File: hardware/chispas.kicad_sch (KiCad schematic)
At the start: 25 parts, among them J1 Conn_01x05, J2 Conn_01x04, J3 Conn_01x04, J4 Conn_01x06, J5 Conn_01x02, U1 Heltec_WiFi_LoRa_32_V3, U2 PC817X2CSP9F, U3 PAM8302AASCR

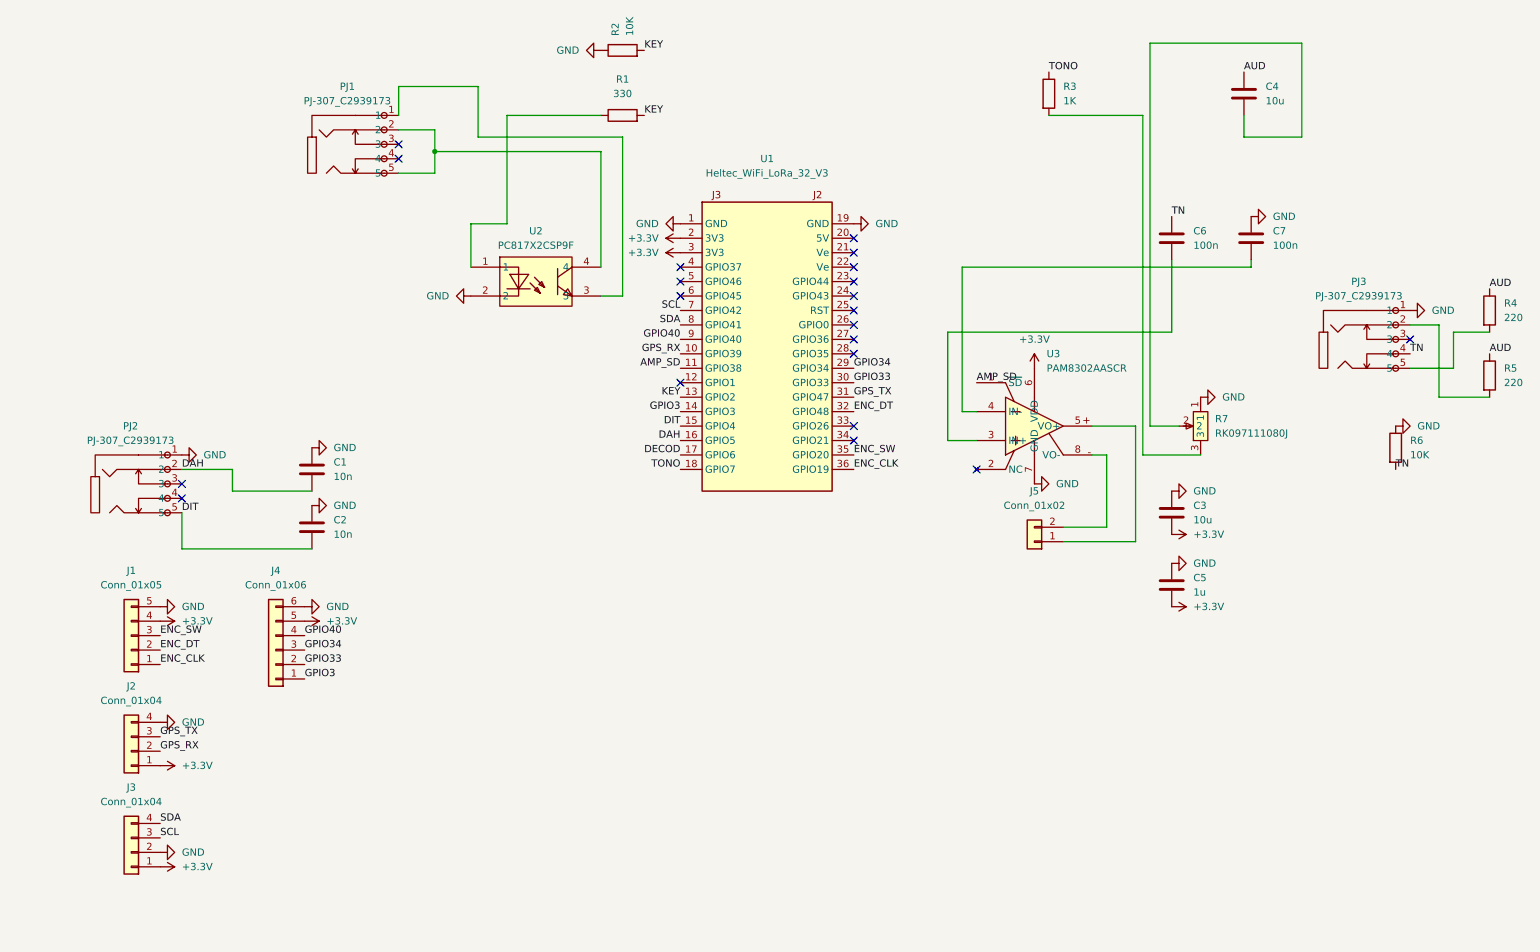
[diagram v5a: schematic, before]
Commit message: PCB: esquema completo (decodificador con puentes para trafo; ERC sin avisos)
Co-Authored-By: Claude Opus 5.5 <noreply@anthropic.com>
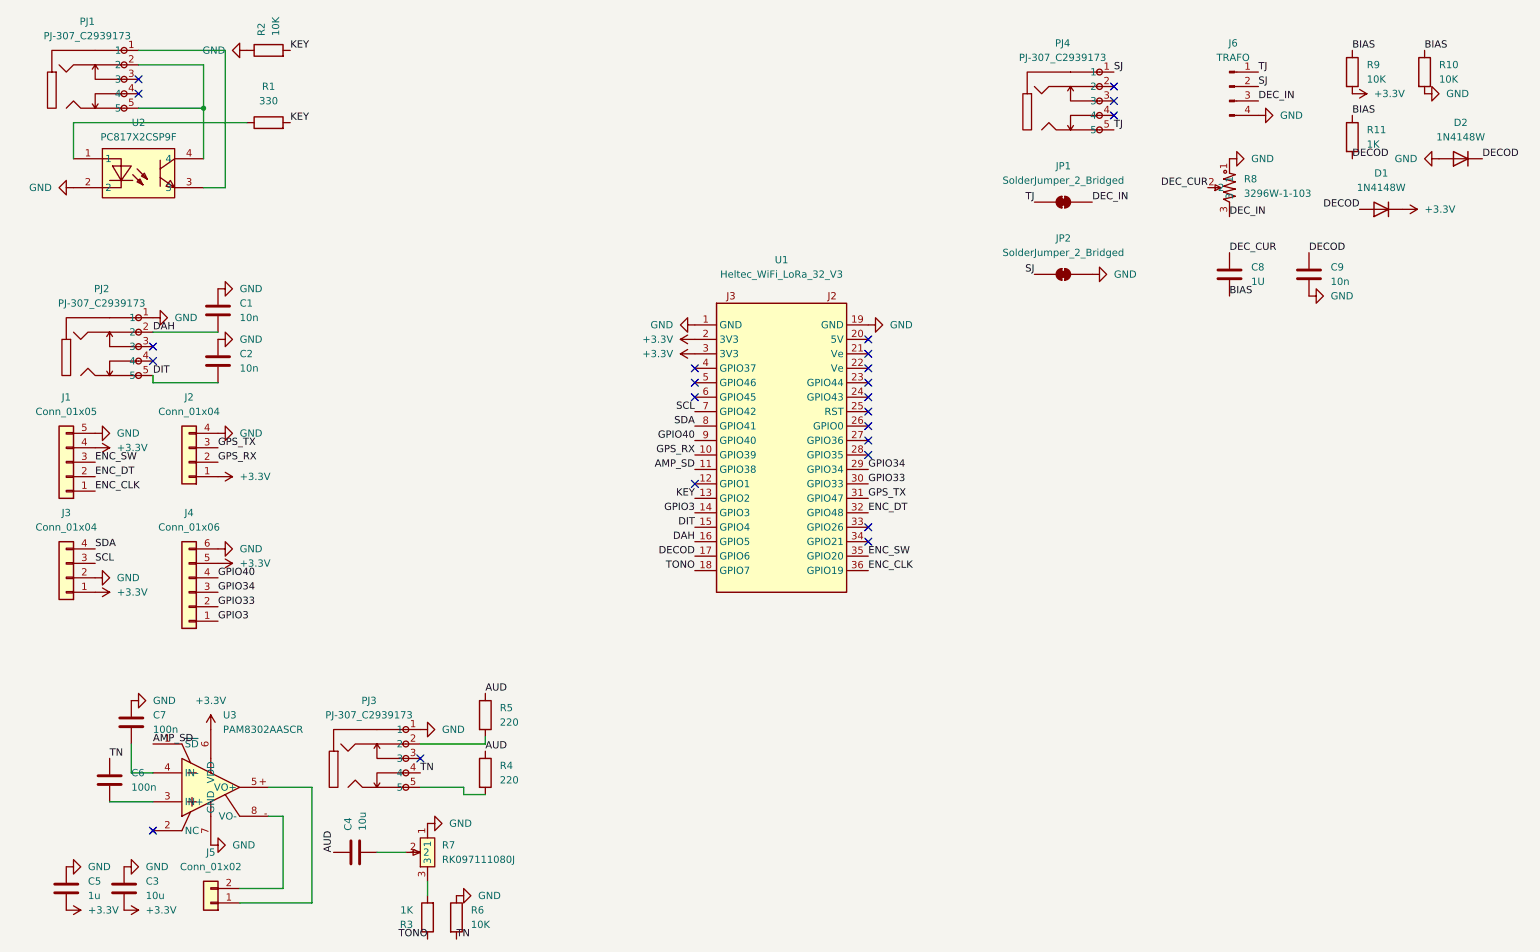
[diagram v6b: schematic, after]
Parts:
- added C8: 1U, Capacitor_SMD:C_0805_2012Metric, symbol Device:C
- added C9: 10n, Capacitor_SMD:C_0805_2012Metric, symbol Device:C
- added D1, D2: 1N4148W, Diode_SMD:D_SOD-123, symbol Device:D
- added J6: TRAFO, Connector_PinHeader_2.54mm:PinHeader_1x04_P2.54mm_Vertical, symbol Connector:Conn_01x04_Pin
- added JP1, JP2: SolderJumper_2_Bridged, Jumper:SolderJumper-2_P1.3mm_Bridged_RoundedPad1.0x1.5mm, symbol Jumper:SolderJumper_2_Bridged
- added PJ4: PJ-307_C2939173, chispas:AUDIO-TH_PJ-307, symbol chispas:PJ-307_C2939173
- added R10, R9: 10K, Resistor_SMD:R_0805_2012Metric, symbol Device:R
- added R11: 1K, Resistor_SMD:R_0805_2012Metric, symbol Device:R
- added R8: 3296W-1-103, chispas:RES-ADJ-TH_3P-L10.0-W10.0-P2.50-L, symbol chispas:3296W-1-103
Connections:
- net +3.3V: now also D1.1 (K), R9.2
- net DECOD: now also C9.1, D1.2 (A), D2.1 (K), R11.2
- net GND: now also C9.2, D2.2 (A), J6.4 (Pin_4), JP2.2 (B), R10.2, R8.1
- new net BIAS: C8.2, R10.1, R11.1, R9.1
- new net DEC_CUR: C8.1, R8.2
- new net DEC_IN: J6.3 (Pin_3), JP1.2 (B), R8.3
- new net SJ: J6.2 (Pin_2), JP2.1 (A), PJ4.1
- new net TJ: J6.1 (Pin_1), JP1.1 (A), PJ4.5
- no-connect marks 21 -> 24
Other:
- moved on the sheet: C1, C2, C3, C4, C5, C6, C7, J1, J2, J3, J4, J5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

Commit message: PCB: placa de 90x60 mm, primera colocacion (colocar.py) y agujeros de los jacks sin metalizar
Co-Authored-By: Claude Opus 5.5 <noreply@anthropic.com>
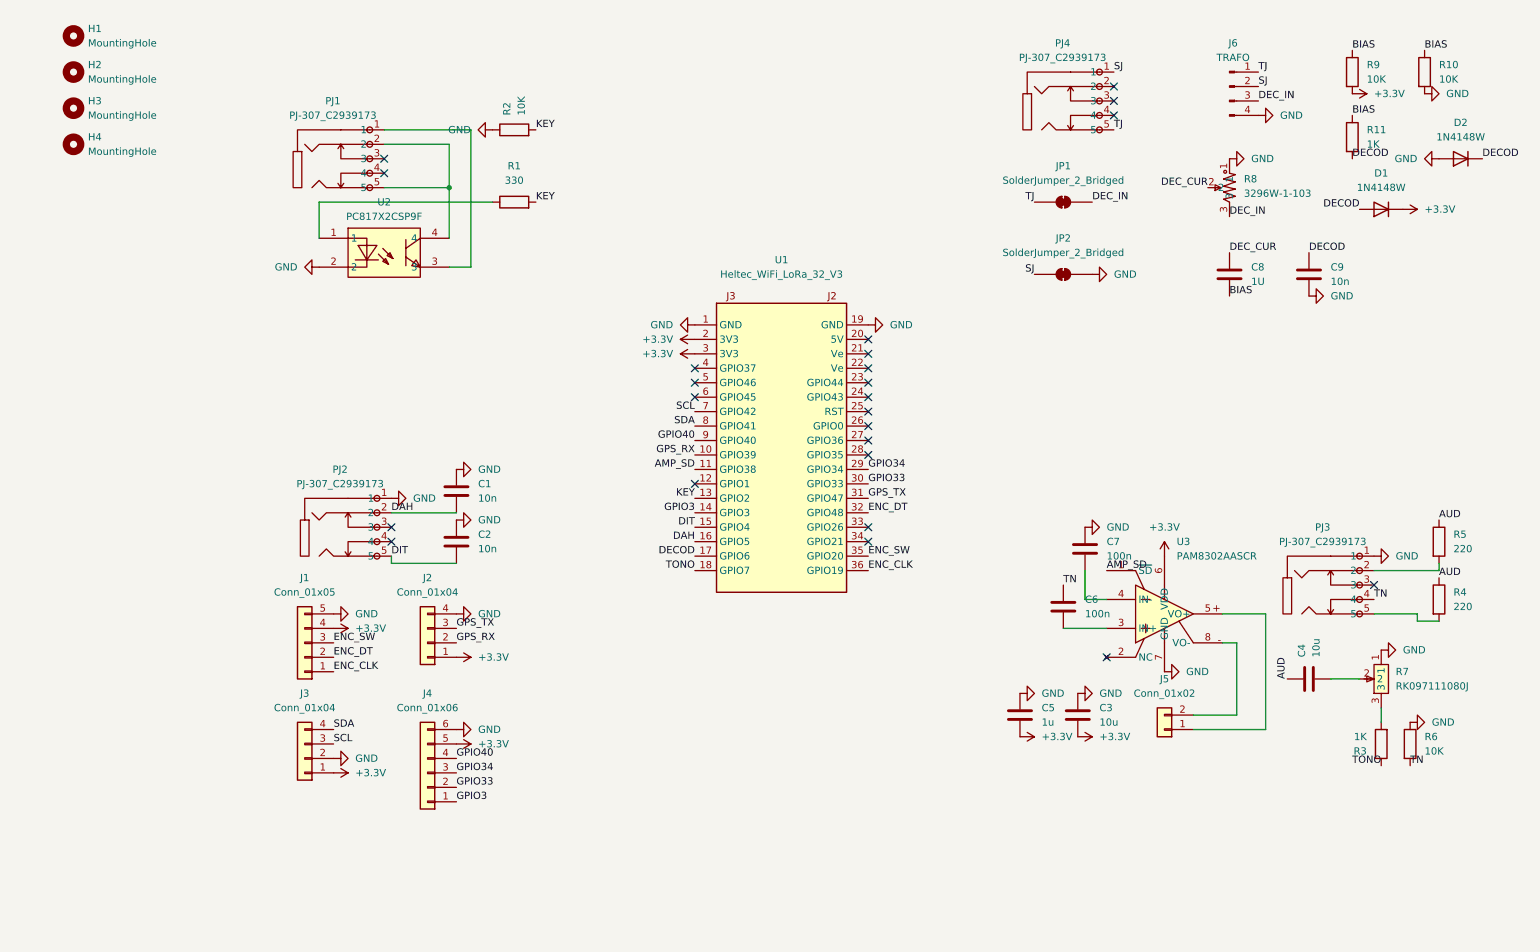
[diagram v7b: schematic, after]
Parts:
- added H1, H2, H3, H4: MountingHole, MountingHole:MountingHole_3.2mm_M3, symbol Mechanical:MountingHole
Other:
- moved on the sheet: C1, C2, C3, C4, C5, C6, C7, J1, J2, J3, J4, J5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

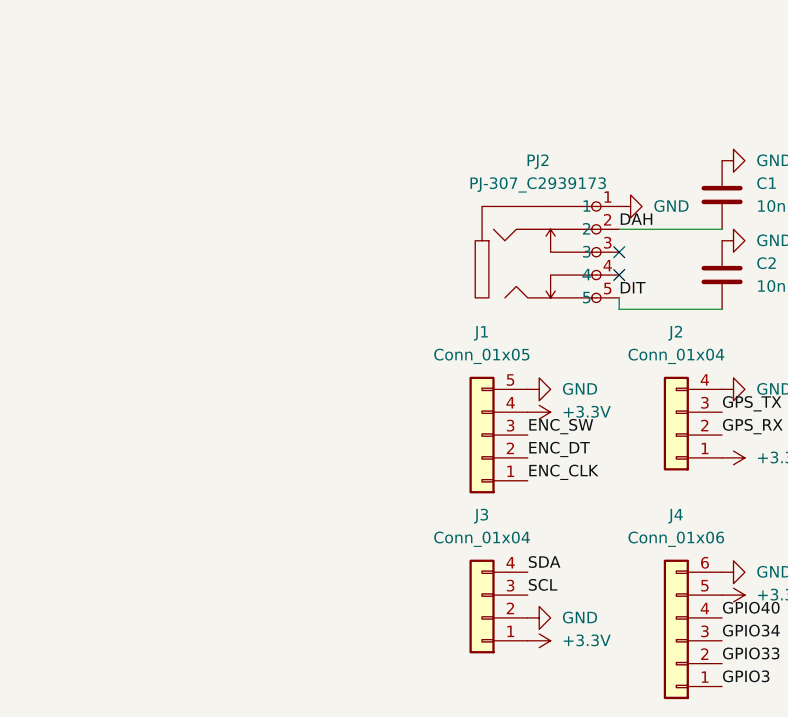
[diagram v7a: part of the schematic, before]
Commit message: PCB: encoder Bourns PEC11R-4230F-S0024 en la placa (24/24, eje 30 mm) con el filtro RC de Bourns; tipos_pines: pasivos por defecto
Co-Authored-By: Claude Opus 5.5 <noreply@anthropic.com>
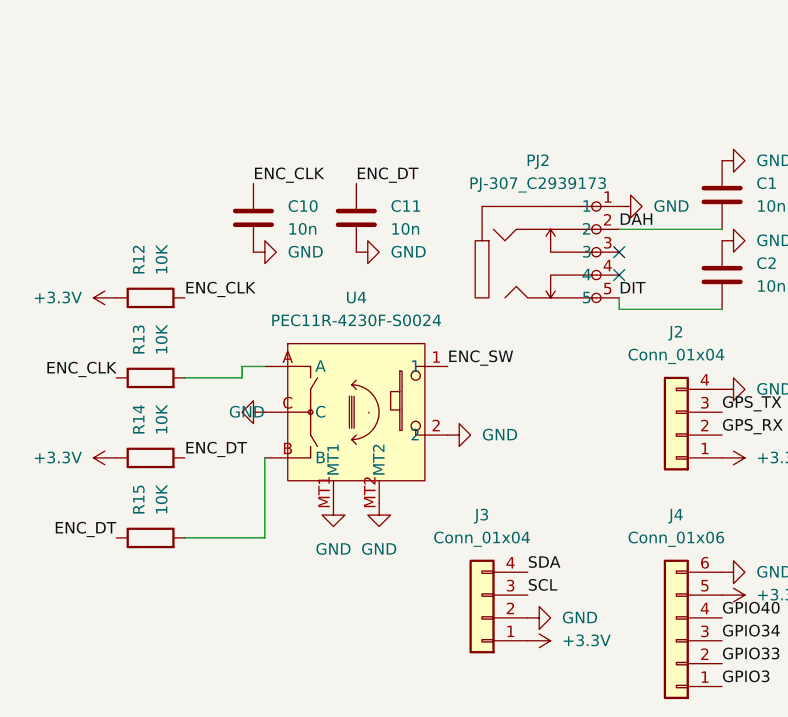
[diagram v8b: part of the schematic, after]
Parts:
- removed J1: Conn_01x05, Connector_JST:JST_XH_B5B-XH-A_1x05_P2.50mm_Vertical, symbol Connector_Generic:Conn_01x05
- added C10, C11: 10n, Capacitor_SMD:C_0805_2012Metric, symbol Device:C
- added R12, R13, R14, R15: 10K, Resistor_SMD:R_0805_2012Metric, symbol Device:R
- added U4: PEC11R-4230F-S0024, chispas:SW-TH_PEC11R-4XXXF-SXXXX, symbol chispas:PEC11R-4230F-S0024
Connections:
- net +3.3V: now also R12.1, R14.1
- net ENC_CLK: now also C10.1, R12.2, R13.1
- net ENC_DT: now also C11.1, R14.2, R15.1
- net ENC_SW: now also U4.1
- net GND: now also C10.2, C11.2, U4.2, U4.C, U4.MT1, U4.MT2
- new net: R15.2, U4.B
- new net: R13.2, U4.A
